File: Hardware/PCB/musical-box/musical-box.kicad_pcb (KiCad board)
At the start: 4 copper layers, 70 x 75 mm, 190 parts, among them J1 power, J201 PSU, J202 Jack-DC, J203 Li Ion 2S, J401 SPI Display, J402 Rotary Encoder 1, J403 I2C Display, J404 Rotary Encoder 2, J405 WS2812, J501 OUT1, J502 OUT2, J503 AudioJack4, P201 USB_C, P202 ICT-Point, P203 ICT-Point, P204 ICT-Point, Q201 DMP3017SFK, Q202 IRF9362, Q203 IRF9362, Q204 IRF9362, Q301 BC846BDW1, SW301 boot, SW302 reset, U201 STUSB4500QTR, U202 MP2615, U203 TPS56339, U204 TLV75733PDBV, U205 TLV75733PDBV, U206 TLV803EC30DBZR, U207 LTC4412xS6, U208 LTC4412xS6, U301 CH340C, U302 ESP32-WROVER, U401 PCF8574ATS, U501 SPH0644HM4H-1, U502 SPH0644HM4H-1, U503 TAS5754MDCA

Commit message: Further work on the layout
Get back to diodes, since they are cheaper
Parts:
- removed Q202, Q203: IRF9362, Package_SO:SOIC-8_3.9x4.9mm_P1.27mm
- removed U207, U208: LTC4412xS6, Package_TO_SOT_SMD:TSOT-23-6
- added D201: NTS1045EMFST1G, SilentWorks:DIO_NTS1045EMFST1G, B.Cu at (402.5, 139.4)
- added D204: NTS1045EMFST1G, SilentWorks:DIO_NTS1045EMFST1G, F.Cu at (392.3, 139.4)
- added G***: LOGO, SilentWorks:logo, B.Cu at (392.6, 171.2)
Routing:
- net Net-(D201-Pad2): track 14.2 -> 0.00 mm
- net Net-(Q203-Pad2): track 10.1 -> 0.00 mm
- net Net-(Q202-Pad2): track 10.0 -> 0.00 mm
- net Net-(C212-Pad2): track 18.3 -> 9.77 mm
- net VDC: track 33.8 -> 30.1 mm, vias 22 -> 37
- net GND: track 103.5 -> 102.7 mm
- removed copper zone on B.Cu, net Net-(Q202-Pad1)
- removed copper zone on F.Cu, net Net-(Q203-Pad1)
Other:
- board text added: "JLCJLCJLCJLC"

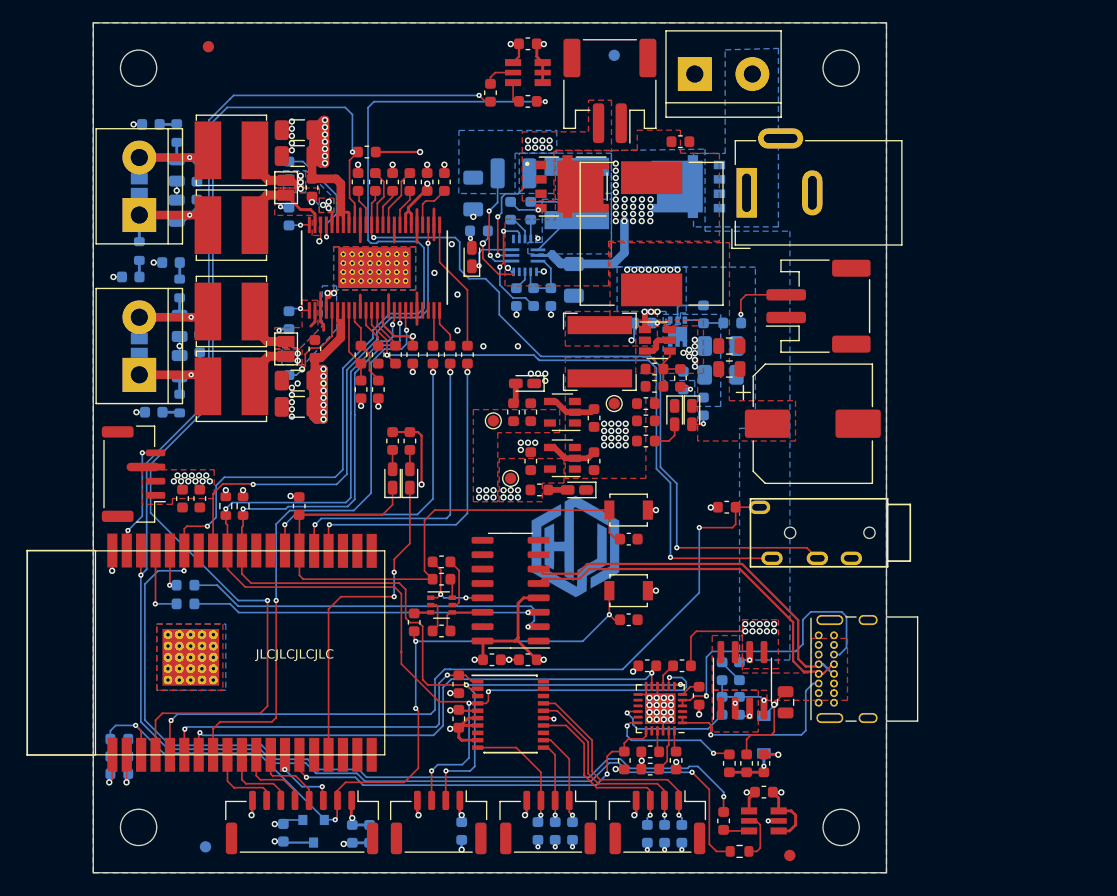
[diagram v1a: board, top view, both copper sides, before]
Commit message: Reduce PCB by 15mm on one edge
New PCB size is 70x60mm through better positioning and higher packing
ratio.
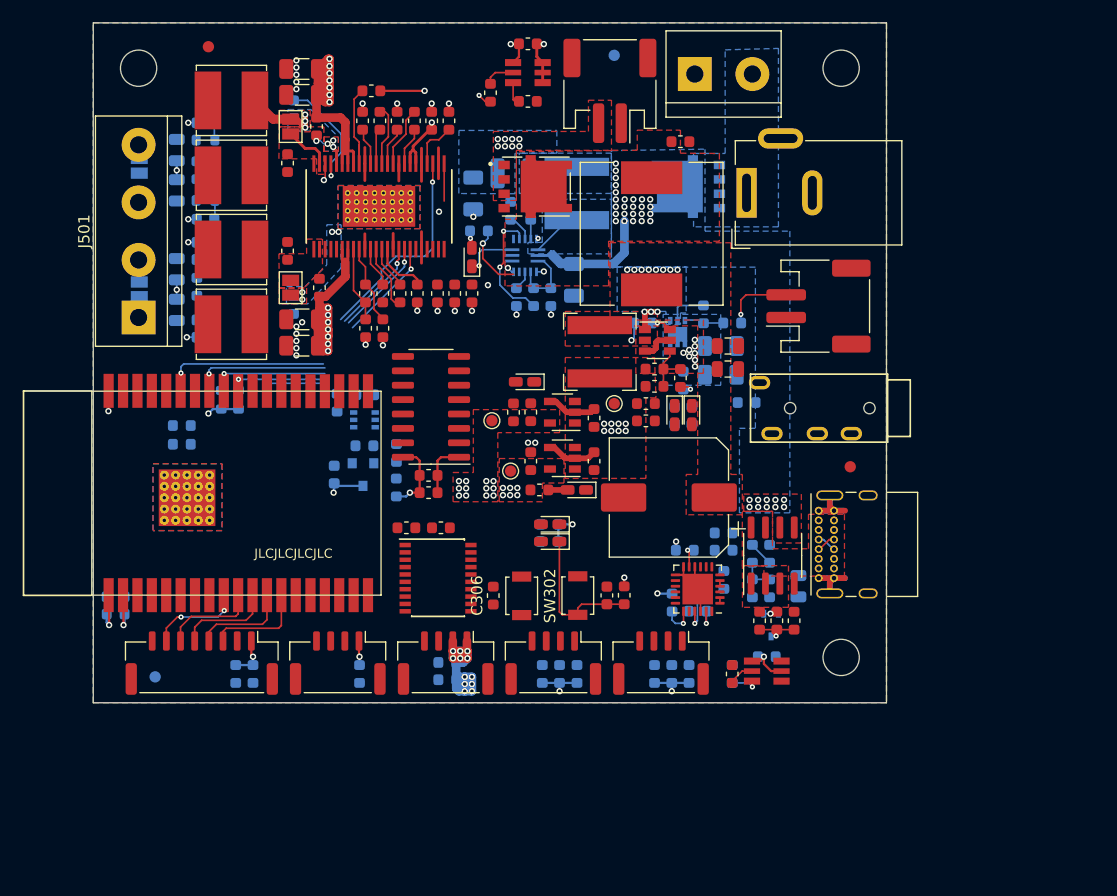
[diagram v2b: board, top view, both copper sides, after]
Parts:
- removed D202: PMEG6010CEH, Diode_SMD:D_SOD-123
- removed G***: LOGO, SilentWorks:logo
- removed H103: MountingHole, MountingHole:MountingHole_3.2mm_M3
- removed J502: OUT2, TerminalBlock:TerminalBlock_bornier-2_P5.08mm
- added D1: BAT54W, Package_TO_SOT_SMD:SOT-323_SC-70, B.Cu at (409.8, 178.1)
- C203, C204, C208, C209, C405, C406, C502, Q301, R104, R105, R106, R107, R209, R210, R213, R214, R218, R304, R305, R308, R309, R501, R509: moved to B.Cu
- C513, C515: moved to F.Cu
- J501: value OUT1 -> spk_out; footprint TerminalBlock:TerminalBlock_bornier-2_P5.08mm -> TerminalBlock:TerminalBlock_bornier-4_P5.08mm
- moved FID103 34.7 mm to (416.8, 164.2)
- moved R222 33.0 mm to (376.7, 166.0), turned to 90 degrees
- moved J405 32.2 mm to (381.1, 181.5), turned to 180 degrees
- moved C227 31.9 mm to (371.3, 164.9)
- moved U206 31.8 mm to (373.8, 164.9)
- moved R312 29.7 mm to (396.9, 175.5)
- moved C405 27.5 mm to (381.2, 181.4), turned to 180 degrees
- moved C406 27.1 mm to (381.2, 183.0), turned to 180 degrees
- moved C302 18.5 mm to (379.6, 164.9), turned to 0 degrees
- moved R309 18.1 mm to (371.5, 158.5), turned to 270 degrees
- moved Q301 17.7 mm to (373.9, 160.0), turned to 180 degrees
- moved R308 17.7 mm to (373.9, 162.3), turned to 180 degrees
- moved U301 17.7 mm to (379.8, 158.9)
- moved C401 17.5 mm to (362.6, 182.5)
- moved C402 17.5 mm to (364.1, 182.5)
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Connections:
- C511 pad 1: Net-(C511-Pad1) -> /Audio Output/DAC_OUTA
- C511 pad 2: /Audio Output/DAC_OUTA -> Net-(C511-Pad2)
- C525 pad 1: /Audio Output/DAC_OUTB -> Net-(C525-Pad1)
- C525 pad 2: Net-(C525-Pad2) -> /Audio Output/DAC_OUTB
- J403 pad 2: /Microcontroller/IO05 -> /Microcontroller/IO18
- J403 pad 3: /Microcontroller/IO18 -> /Microcontroller/IO05
- P201 pad A8: (no net) -> Net-(P201-PadA8)
- P201 pad B8: (no net) -> Net-(P201-PadB8)
- U201 pad 14: (no net) -> Net-(U201-Pad14)
- U201 pad 15: (no net) -> Net-(U201-Pad15)
- U201 pad 17: (no net) -> Net-(U201-Pad17)
- U201 pad 20: (no net) -> Net-(U201-Pad20)
- U201 pad 3: (no net) -> Net-(U201-Pad3)
- U202 pad 12: (no net) -> Net-(U202-Pad12)
- U301 pad 10: (no net) -> Net-(U301-Pad10)
- U301 pad 11: (no net) -> Net-(U301-Pad11)
- U301 pad 12: (no net) -> Net-(U301-Pad12)
- U301 pad 15: (no net) -> Net-(U301-Pad15)
- U301 pad 7: (no net) -> Net-(U301-Pad7)
- U301 pad 8: (no net) -> Net-(U301-Pad8)
- U301 pad 9: (no net) -> Net-(U301-Pad9)
- U302 pad 17: (no net) -> Net-(U302-Pad17)
- U302 pad 18: (no net) -> Net-(U302-Pad18)
- U302 pad 19: (no net) -> Net-(U302-Pad19)
- U302 pad 20: (no net) -> Net-(U302-Pad20)
- U302 pad 21: (no net) -> Net-(U302-Pad21)
- U302 pad 22: (no net) -> Net-(U302-Pad22)
- U401 pad 13: (no net) -> Net-(U401-Pad13)
- U401 pad 18: (no net) -> Net-(U401-Pad18)
- U401 pad 19: (no net) -> Net-(U401-Pad19)
- U401 pad 20: (no net) -> Net-(U401-Pad20)
- U401 pad 3: (no net) -> Net-(U401-Pad3)
- U401 pad 8: (no net) -> Net-(U401-Pad8)
- U503 pad 12: /Audio Output/DAC_OUTA -> Net-(C511-Pad2)
- U503 pad 13: Net-(C511-Pad1) -> /Audio Output/DAC_OUTA
- U503 pad 19: (no net) -> /Audio Output/GPIO1
- U503 pad 21: (no net) -> /Audio Output/GPIO2
- U503 pad 22: (no net) -> Net-(U503-Pad22)
- U503 pad 36: Net-(C525-Pad2) -> /Audio Output/DAC_OUTB
- U503 pad 37: /Audio Output/DAC_OUTB -> Net-(C525-Pad1)
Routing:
- net /Microcontroller/IO22: track 144.7 -> 1.23 mm, vias 3 -> 1
- net /Microcontroller/IO21: track 152.1 -> 14.8 mm, vias 4 -> 1
- net /Microcontroller/I36: track 98.5 -> 8.58 mm, vias 2 -> 0
- net /Microcontroller/IO18: track 99.7 -> 20.3 mm, vias 6 -> 2
- net /Microcontroller/IO05: track 96.6 -> 18.2 mm, vias 5 -> 2
- net /Microcontroller/~RESET: track 71.3 -> 0.00 mm, vias 5 -> 0
- net /Audio Output/Detect: track 68.7 -> 0.00 mm, vias 2 -> 0
- net +5V: track 0.00 -> 65.4 mm, vias 27 -> 20
- net /Audio Output/DAC_OUTB: track 66.3 -> 5.40 mm, vias 2 -> 0
- net /Audio Output/DAC_OUTA: track 56.0 -> 3.79 mm, vias 2 -> 0
- net /Microcontroller/I35: track 48.2 -> 2.06 mm, vias 2 -> 1
- net /Microcontroller/IO00: track 52.7 -> 12.8 mm
- net /Audio Output/GPIO0: track 53.2 -> 14.6 mm, vias 2 -> 1
- net Net-(R302-Pad2): track 33.6 -> 0.00 mm, vias 1 -> 0
- net /Microcontroller/IO12: track 36.1 -> 2.84 mm, vias 2 -> 1
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- removed copper zone on In1.Cu, net +5V
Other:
- board size 70 x 75 mm -> 70 x 60 mm
- net class 1A: via_dia 0.46 -> 0.56; via_drill 0.2 -> 0.3
- net class 3A: via_dia 0.46 -> 0.56; via_drill 0.2 -> 0.3

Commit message: No unconnected nets any more
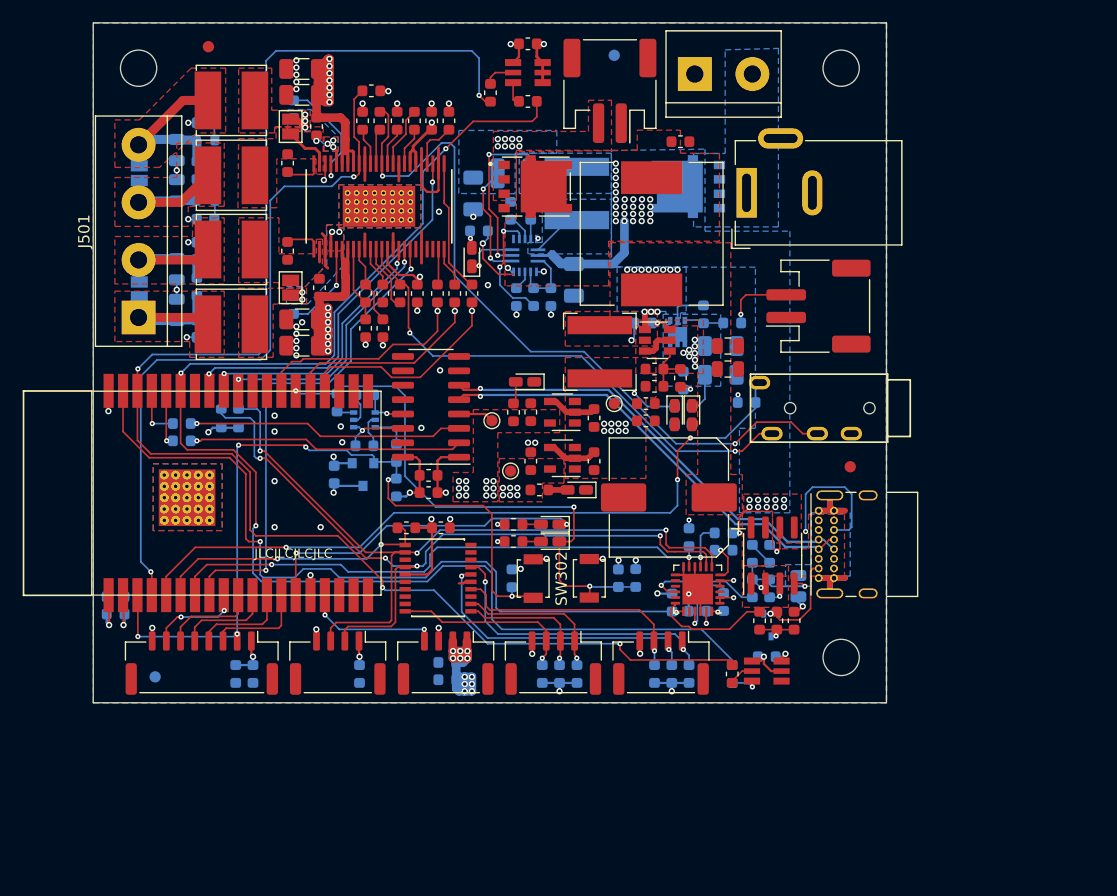
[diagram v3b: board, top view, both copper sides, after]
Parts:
- C305, C306, R312: moved to B.Cu
- R104, R105: moved to F.Cu
- moved R104 3.18 mm to (387.1, 169.3), turned to 180 degrees
- moved R105 3.18 mm to (387.1, 170.8), turned to 180 degrees
- moved C306 2.25 mm to (386.9, 174.0)
- moved C204 1.95 mm to (405.6, 176.1), turned to 90 degrees
- moved R312 1.83 mm to (397.9, 174.0)
- moved SW302 1.83 mm to (388.8, 174.0)
- moved C305 1.83 mm to (396.3, 174.0)
- moved SW301 1.83 mm to (393.8, 174.0)
- moved R303 1.82 mm to (357.8, 160.4)
- moved R106 1.65 mm to (362.8, 159.9)
- moved R107 1.65 mm to (361.3, 159.9)
- moved R302 1.35 mm to (357.8, 161.9)
- moved R214 1.20 mm to (402.6, 170.4), turned to 270 degrees
- moved JP4 0.66 mm to (354.1, 138.3)
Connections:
- D101 pad 1: /Microcontroller/IO13 -> /Microcontroller/IO12
- J401 pad MP: (no net) -> GND
- J402 pad MP: (no net) -> GND
- J403 pad MP: (no net) -> GND
- J404 pad MP: (no net) -> GND
- J405 pad 4: /Microcontroller/IO23 -> /Microcontroller/IO13
- J405 pad MP: (no net) -> GND
- R213 pad 2: /Microcontroller/IO12 -> /Microcontroller/IO23
- R509 pad 2: +3V3 -> +3.3VA
- U201 pad 19: /Microcontroller/IO12 -> /Microcontroller/IO23
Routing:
- net /Microcontroller/IO22: track 1.23 -> 132.3 mm, vias 1 -> 4
- net /Microcontroller/IO21: track 14.8 -> 119.4 mm, vias 1 -> 3
- net /Microcontroller/IO05: track 18.2 -> 92.3 mm, vias 2 -> 5
- net /Microcontroller/IO18: track 20.3 -> 94.4 mm, vias 2 -> 6
- net /Microcontroller/~RESET: track 0.00 -> 69.9 mm, vias 0 -> 6
- net /Microcontroller/IO23: track 0.00 -> 68.4 mm, vias 0 -> 2
- net /Audio Output/Detect: track 0.00 -> 65.0 mm, vias 0 -> 3
- net /Audio Output/DAC_OUTB: track 5.40 -> 64.9 mm, vias 0 -> 2
- net /Microcontroller/I36: track 8.58 -> 63.6 mm, vias 0 -> 2
- net /Microcontroller/I35: track 2.06 -> 49.6 mm, vias 1 -> 2
- net /Audio Output/DAC_OUTA: track 3.79 -> 45.6 mm, vias 0 -> 2
- net /Microcontroller/D-: track 1.70 -> 39.4 mm, vias 0 -> 1
- net /Microcontroller/D+: track 1.70 -> 39.4 mm, vias 0 -> 1
- net /Microcontroller/IO00: track 12.8 -> 49.4 mm, vias 0 -> 3
- net GND: track 97.8 -> 128.3 mm, vias 43 -> 68
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- added copper zone on F.Cu, net /Audio Output/OUT1+
- added copper zone on F.Cu, net /Audio Output/OUT1-
- added copper zone on F.Cu, net /Audio Output/OUT2+
- added copper zone on F.Cu, net /Audio Output/OUT2-
- added copper zone on B.Cu, net Net-(C203-Pad2)

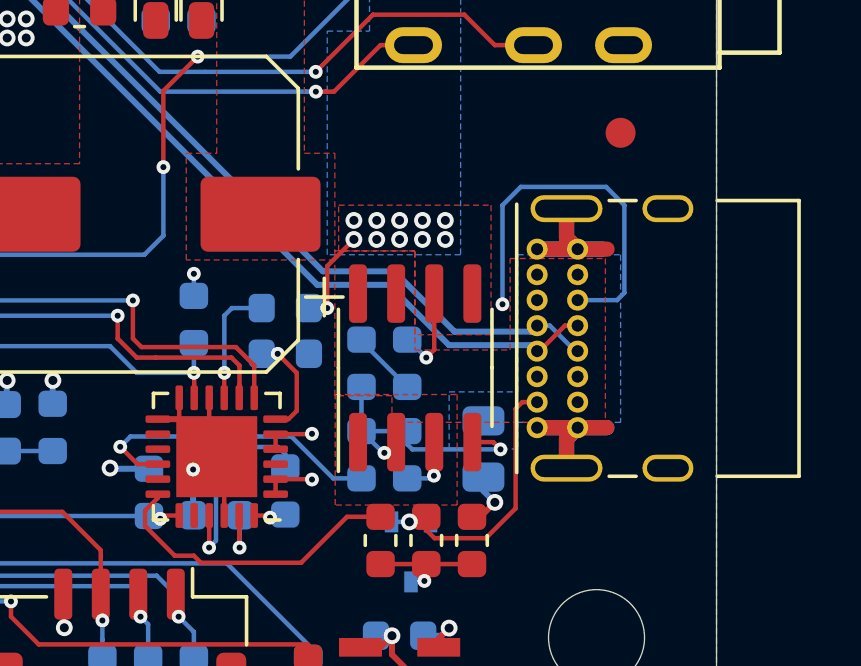
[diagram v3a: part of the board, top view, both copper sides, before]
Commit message: Layout optimizations
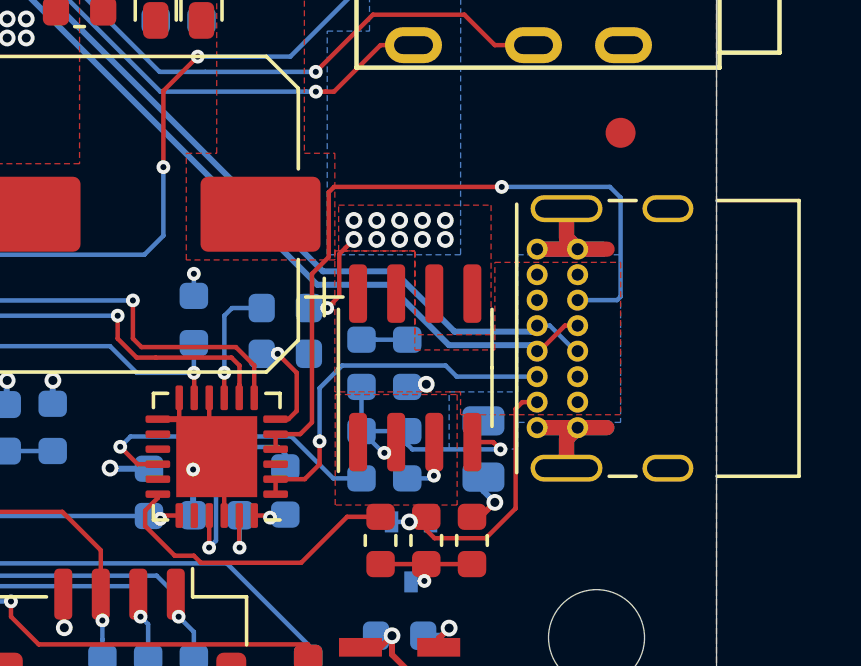
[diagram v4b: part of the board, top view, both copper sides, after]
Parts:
- turned C205 to 270 degrees
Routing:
- net VDC: track 27.2 -> 29.7 mm
- net Net-(P201-PadA5): track 10.6 -> 12.4 mm
- net Net-(P201-PadB5): track 23.6 -> 24.5 mm, vias 2 -> 1
- net Net-(C205-Pad1): track 2.21 -> 1.52 mm

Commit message: Layout optimisations
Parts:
- removed JP1, JP2: mono, Jumper:SolderJumper-2_P1.3mm_Open_Pad1.0x1.5mm
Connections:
- U503 pad 22: Net-(U503-Pad22) -> /Audio Output/GPIO2
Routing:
- net /Audio Output/GPIO2: track 0.00 -> 2.42 mm
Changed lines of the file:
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@@
     (thickness 1.6)
     (drawings 7)
-    (tracks 1597)
+    (tracks 1602)
     (zones 0)
-    (modules 186)
-    (nets 151)
+    (modules 184)
+    (nets 150)
   )
   (page A4)
@@
   (net 145 "Net-(U401-Pad8)")
   (net 146 "Net-(U401-Pad3)")
-  (net 147 "Net-(U503-Pad22)")
-  (net 148 "/Audio Output/GPIO2")
-  (net 149 "/Audio Output/GPIO1")
-  (net 150 "Net-(D1-Pad2)")
+  (net 147 "/Audio Output/GPIO2")
+  (net 148 "/Audio Output/GPIO1")
+  (net 149 "Net-(D1-Pad2)")
   (net_class Default "This is the default net class."
     (clearance 0.2)
@@
     (add_net "Net-(U401-Pad3)")
     (add_net "Net-(U401-Pad8)")
-    (add_net "Net-(U503-Pad22)")
   )
   (net_class 1A ""
@@
       (net 33 "Net-(C210-Pad2)"))
     (pad 2 smd rect (at -1 -0.65) (size 0.45 0.7) (layers B.Cu B.Paste B.Mask)
-      (net 150 "Net-(D1-Pad2)"))
+      (net 149 "Net-(D1-Pad2)"))
     (pad 1 smd rect (at -1 0.65) (size 0.45 0.7) (layers B.Cu B.Paste B.Mask)
       (net 27 "Net-(C203-Pad2)"))
@@
       (net 102 "/Audio Output/OUT1-"))
   )
-  (module Jumper:SolderJumper-2_P1.3mm_Open_Pad1.0x1.5mm (layer F.Cu)
-    (at 367.418 134.148 90)
-    (descr "SMD Solder Jumper, 1x1.5mm Pads, 0.3mm gap, open")
-    (tags "solder jumper open")
-    (attr virtual)
-    (fp_text reference JP2 (at 0 -1.8 90) (layer F.SilkS) hide
-      (effects (font (size 1 1) (thickness 0.15)))
-    )
-    (fp_text value mono (at 0 1.9 90) (layer F.Fab) hide
-      (effects (font (size 1 1) (thickness 0.15)))
-    )
-    (fp_line (start 1.65 1.25) (end -1.65 1.25) (layer F.CrtYd) (width 0.05))
-    (fp_line (start 1.65 1.25) (end 1.65 -1.25) (layer F.CrtYd) (width 0.05))
-    (fp_line (start -1.65 -1.25) (end -1.65 1.25) (layer F.CrtYd) (width 0.05))
-    (fp_line (start -1.65 -1.25) (end 1.65 -1.25) (layer F.CrtYd) (width 0.05))
-    (fp_line (start -1.4 -1) (end 1.4 -1) (layer F.SilkS) (width 0.12))
-    (fp_line (start 1.4 -1) (end 1.4 1) (layer F.SilkS) (width 0.12))
-    (fp_line (start 1.4 1) (end -1.4 1) (layer F.SilkS) (width 0.12))
-    (fp_line (start -1.4 1) (end -1.4 -1) (layer F.SilkS) (width 0.12))
-    (pad 1 smd rect (at -0.65 0 90) (size 1 1.5) (layers F.Cu F.Mask)
-      (net 104 "/Audio Output/SPKB_OUT+"))
-    (pad 2 smd rect (at 0.65 0 90) (size 1 1.5) (layers F.Cu F.Mask)
-      (net 107 "/Audio Output/SPKB_OUT-"))
-  )
-  (module Jumper:SolderJumper-2_P1.3mm_Open_Pad1.0x1.5mm (layer F.Cu)
-    (at 367.418 148.372 90)
-    (descr "SMD Solder Jumper, 1x1.5mm Pads, 0.3mm gap, open")
-    (tags "solder jumper open")
-    (attr virtual)
-    (fp_text reference JP1 (at 0 -1.8 90) (layer F.SilkS) hide
-      (effects (font (size 1 1) (thickness 0.15)))
-    )
-    (fp_text value mono (at 0 1.9 90) (layer F.Fab) hide
-      (effects (font (size 1 1) (thickness 0.15)))
-    )
-    (fp_line (start 1.65 1.25) (end -1.65 1.25) (layer F.CrtYd) (width 0.05))
-    (fp_line (start 1.65 1.25) (end 1.65 -1.25) (layer F.CrtYd) (width 0.05))
-    (fp_line (start -1.65 -1.25) (end -1.65 1.25) (layer F.CrtYd) (width 0.05))
-    (fp_line (start -1.65 -1.25) (end 1.65 -1.25) (layer F.CrtYd) (width 0.05))
-    (fp_line (start -1.4 -1) (end 1.4 -1) (layer F.SilkS) (width 0.12))
-    (fp_line (start 1.4 -1) (end 1.4 1) (layer F.SilkS) (width 0.12))
-    (fp_line (start 1.4 1) (end -1.4 1) (layer F.SilkS) (width 0.12))
-    (fp_line (start -1.4 1) (end -1.4 -1) (layer F.SilkS) (width 0.12))
-    (pad 1 smd rect (at -0.65 0 90) (size 1 1.5) (layers F.Cu F.Mask)
-      (net 100 "/Audio Output/SPKA_OUT+"))
-    (pad 2 smd rect (at 0.65 0 90) (size 1 1.5) (layers F.Cu F.Mask)
-      (net 103 "/Audio Output/SPKA_OUT-"))
-  )
   (module Resistor_SMD:R_0603_1608Metric (layer B.Cu)
     (at 359.906 135.343 180)
@@
       (net 19 "/Audio Output/SCLK"))
     (pad 22 smd rect (at -3.775001 4.750001 90) (size 1.4612 0.27) (layers F.Cu F.Paste F.Mask)
-      (net 147 "Net-(U503-Pad22)"))
+      (net 147 "/Audio Output/GPIO2"))
     (pad 21 smd rect (at -3.775001 4.249999 90) (size 1.4612 0.27) (layers F.Cu F.Paste F.Mask)
-      (net 148 "/Audio Output/GPIO2"))
+      (net 147 "/Audio Output/GPIO2"))
     (pad 20 smd rect (at -3.775001 3.75 90) (size 1.4612 0.27) (layers F.Cu F.Paste F.Mask)
       (net 1 GND))
     (pad 19 smd rect (at -3.775001 3.250001 90) (size 1.4612 0.27) (layers F.Cu F.Paste F.Mask)
-      (net 149 "/Audio Output/GPIO1"))
+      (net 148 "/Audio Output/GPIO1"))
     (pad 18 smd rect (at -3.775001 2.75 90) (size 1.4612 0.27) (layers F.Cu F.Paste F.Mask)
       (net 94 "/Audio Output/GPIO0"))
@@
   (segment (start 374.9658 134.7537) (end 375.292 134.4275) (width 0.15) (layer F.Cu) (net 119))
   (segment (start 374.9658 137.421499) (end 374.9658 134.7537) (width 0.15) (layer F.Cu) (net 119))
+  (segment (start 379.465799 145.852101) (end 379.624698 146.011) (width 0.15) (layer F.Cu) (net 147))
+  (segment (start 379.465799 144.971501) (end 379.465799 145.852101) (width 0.15) (layer F.Cu) (net 147))
+  (segment (start 379.624698 146.011) (end 379.845 146.011) (width 0.15) (layer F.Cu) (net 147))
+  (segment (start 379.965801 145.890199) (end 379.965801 144.971501) (width 0.15) (layer F.Cu) (net 147))
+  (segment (start 379.845 146.011) (end 379.965801 145.890199) (width 0.15) (layer F.Cu) (net 147))
   (zone (net 1) (net_name GND) (layer In2.Cu) (hatch edge 0.508)
     (connect_pads thru_hole_only (clearance 0.2))
